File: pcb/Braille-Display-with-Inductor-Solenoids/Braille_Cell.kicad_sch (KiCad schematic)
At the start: 43 parts, among them U10 AD116, U11 AD116, U12 AD116, U13 AD116, U8 AD116, U9 AD116

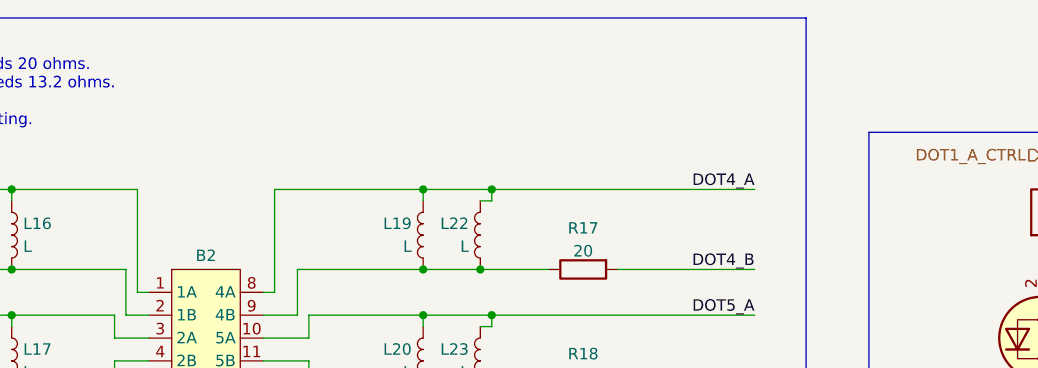
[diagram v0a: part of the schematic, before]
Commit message: Add Rev 2 FIXMEs
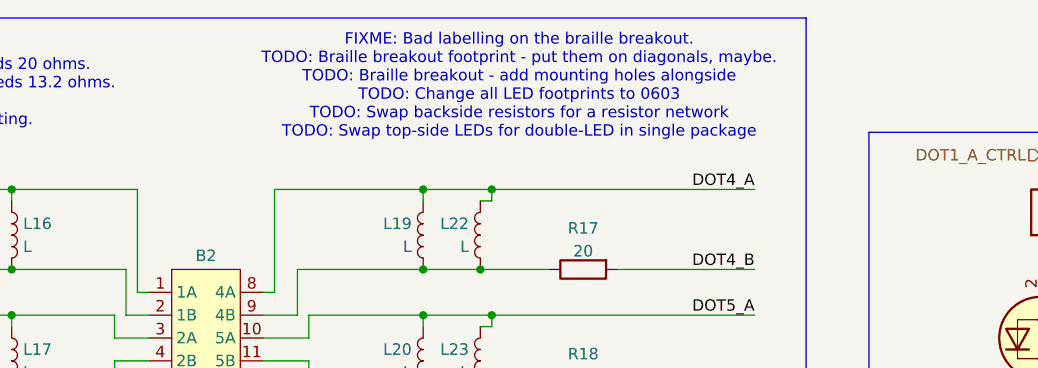
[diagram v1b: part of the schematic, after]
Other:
- note added: "FIXME: Bad labelling on the braille breakout. TODO: Braille breakout footprint - put them on diagonals, maybe. TODO: Braille breakout - add mounting holes alongside TODO: Change all LED footprints to 0603 TODO: Swap backside resistors for a resistor network TODO: Swap top-side LEDs for double-LED in single package"
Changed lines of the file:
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@@
+		)
+	)
+	(text "FIXME: Bad labelling on the braille breakout.\nTODO: Braille breakout footprint - put them on diagonals, maybe.\nTODO: Braille breakout - add mounting holes alongside\nTODO: Change all LED footprints to 0603\nTODO: Swap backside resistors for a resistor network\nTODO: Swap top-side LEDs for double-LED in single package"
+		(exclude_from_sim no)
+		(at 157.988 21.59 0)
+		(effects
+			(font
+				(size 1.27 1.27)
+			)
 		)
 	)

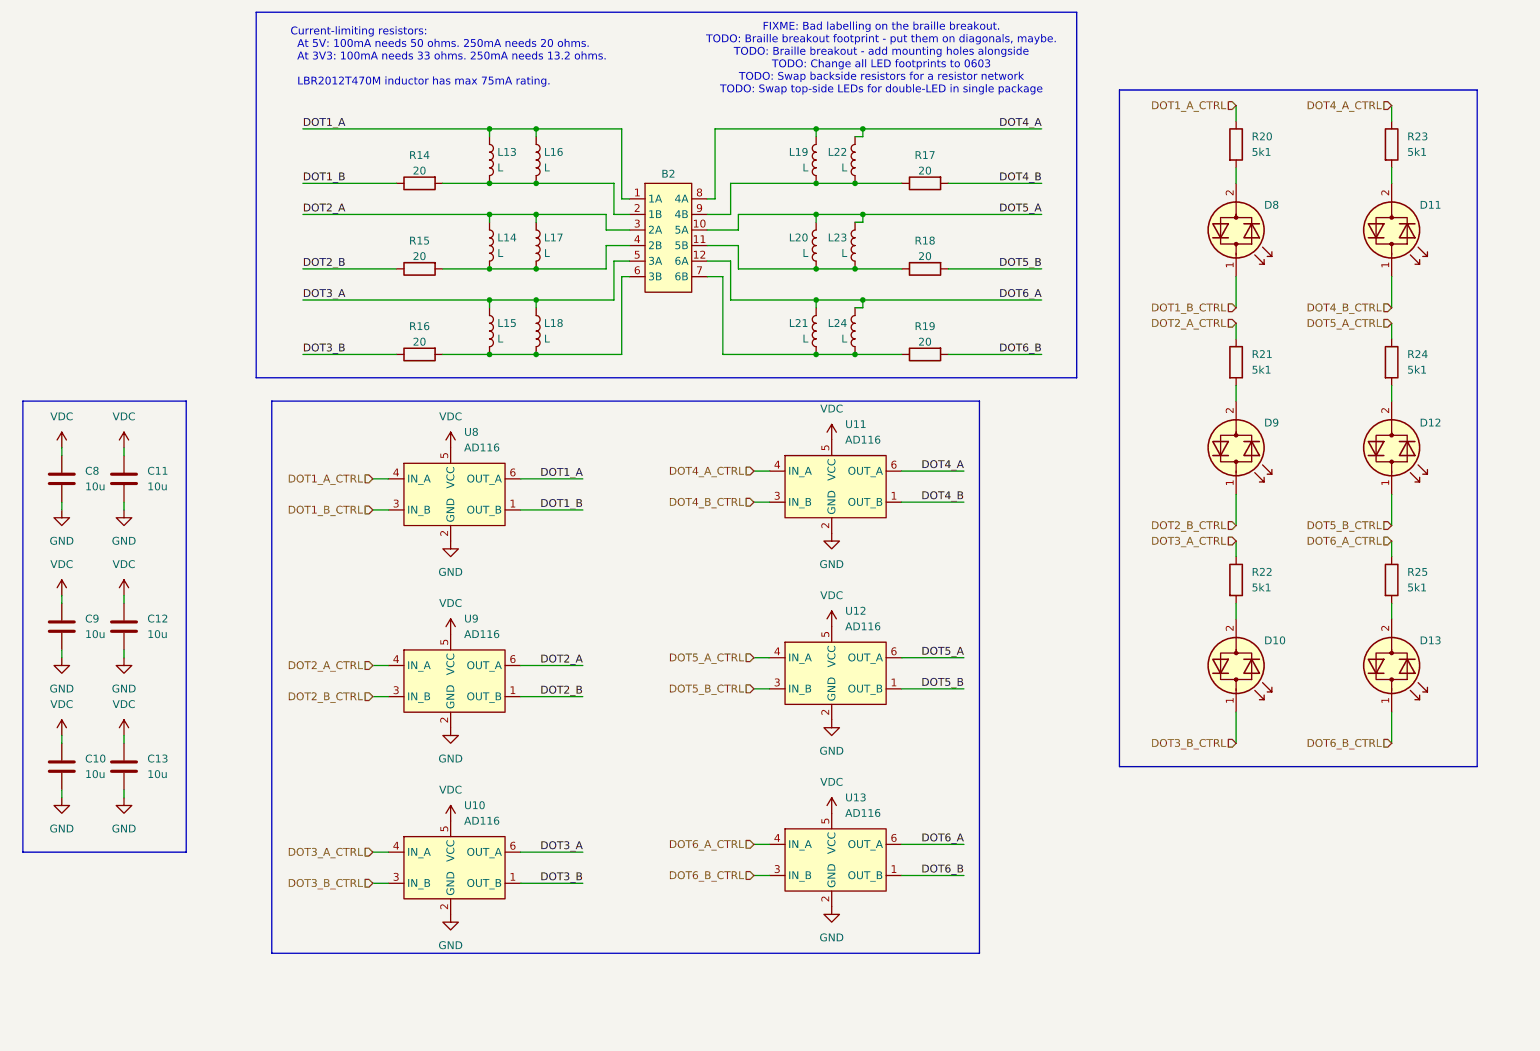
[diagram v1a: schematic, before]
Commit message: WIP (Rev3): Switch to 2 inductors per cell
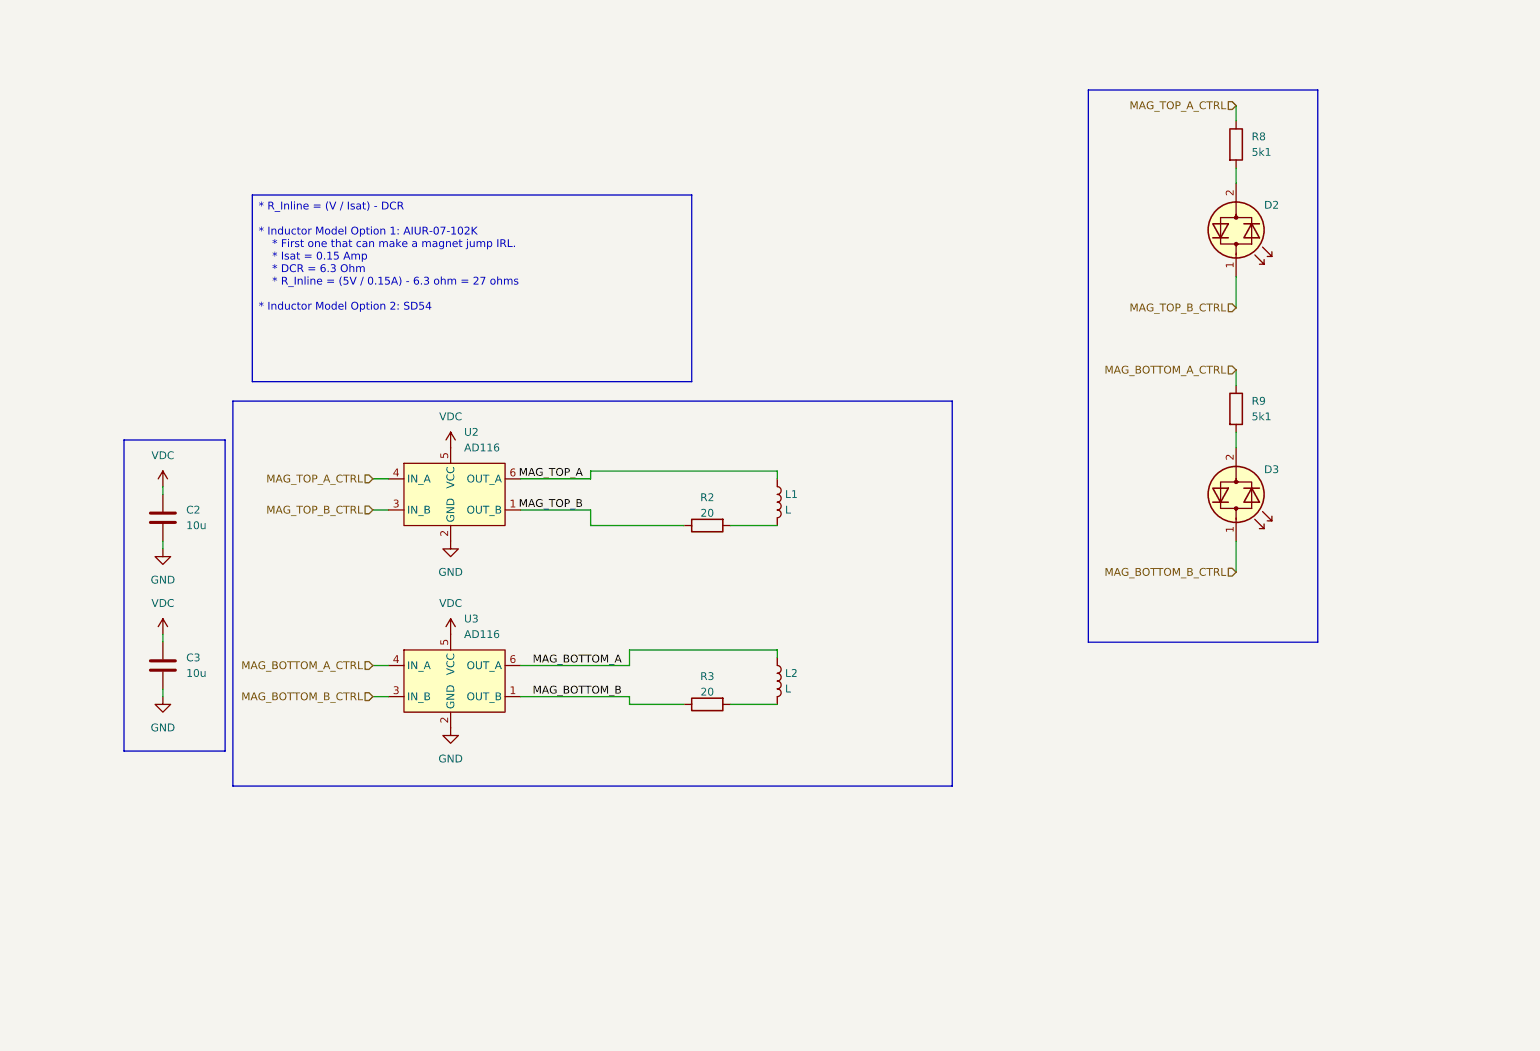
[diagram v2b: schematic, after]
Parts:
- removed B2: ~, 00-project-footprints:Braille_Cell_Breakout, symbol 00-project-symbols:Braille_Cell_Breakout
- removed C10, C11, C12, C13: 10u, Capacitor_SMD:C_1206_3216Metric_Pad1.33x1.80mm_HandSolder, symbol Device:C
- removed D10, D11, D12, D13: LED_Dual_Bidirectional, 00-project-footprints:LED_0603_1608Metric_HandSolder_2x_Reverse, symbol Device:LED_Dual_Bidirectional
- removed L15, L22, L23, L24: L, 00-project-footprints:Inductor_0805_2012Metric_SMD_Vertical_Square_Rev2_1.3mm, symbol Device:L
- removed L16, L17, L18, L19, L20, L21: L, 00-project-footprints:Inductor_VLS201612CX, symbol Device:L
- removed R16, R17, R18, R19: 20, Resistor_SMD:R_0603_1608Metric_Pad0.98x0.95mm_HandSolder, symbol Device:R
- removed R22, R23, R24, R25: 5k1, Resistor_SMD:R_0603_1608Metric_Pad0.98x0.95mm_HandSolder, symbol Device:R
- removed U10, U11, U12, U13: AD116, Package_TO_SOT_SMD:SOT-23-6, symbol 00-project-symbols:AD116_H_Bridge
- L1: renamed from L13; footprint 00-project-footprints:Inductor_0805_2012Metric_SMD_Vertical_Square_Rev2_1.3mm -> 00-project-footprints:Inductor_6mm_AIUR-07-102K_THT_SD54_SMD
- L2: renamed from L14; footprint 00-project-footprints:Inductor_0805_2012Metric_SMD_Vertical_Square_Rev2_1.3mm -> 00-project-footprints:Inductor_6mm_AIUR-07-102K_THT_SD54_SMD
- R2: renamed from R14; footprint Resistor_SMD:R_0603_1608Metric_Pad0.98x0.95mm_HandSolder -> Resistor_SMD:R_2512_6332Metric_Pad1.40x3.35mm_HandSolder
- R3: renamed from R15; footprint Resistor_SMD:R_0603_1608Metric_Pad0.98x0.95mm_HandSolder -> Resistor_SMD:R_2512_6332Metric_Pad1.40x3.35mm_HandSolder
- renumbered C8 to C2, C9 to C3, D8 to D2, D9 to D3, R20 to R8, R21 to R9, U8 to U2, U9 to U3
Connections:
- net DOT1_A renamed MAG_TOP_A
- net DOT1_A_CTRL renamed MAG_TOP_A_CTRL
- net DOT1_B renamed MAG_TOP_B
- net DOT1_B_CTRL renamed MAG_TOP_B_CTRL
- net DOT2_A renamed MAG_BOTTOM_A
- net DOT2_A_CTRL renamed MAG_BOTTOM_A_CTRL
- net DOT2_B renamed MAG_BOTTOM_B
- net DOT2_B_CTRL renamed MAG_BOTTOM_B_CTRL
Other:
- note removed: "Current-limiting resistors: At 5V: 100mA needs 50 ohms. 250mA needs 20 ohms. At 3V3: 100mA needs 33 ohms. 250mA needs 13.2 ohms. LBR2012T470M inductor has max 75mA rating."
- note removed: "FIXME: Bad labelling on the braille breakout. TODO: Braille breakout footprint - put them on diagonals, maybe. TODO: Braille breakout - add mounting holes alongside TODO: Change all LED footprints to 0603 TODO: Swap backside resistors for a resistor network TODO: Swap top-side LEDs for double-LED in single package"
- moved on the sheet: C2, C3, D3, L1, L2, R2, R3, R9

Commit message: WIP: Route one cell
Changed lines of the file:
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@@
+	(wire
+		(pts
+			(xy 87.63 83.82) (xy 87.63 85.09)
+		)
+		(stroke
+			(width 0)
+			(type default)
+		)
+	)
 	(wire
 		(pts
@@
 	(wire
 		(pts
+			(xy 87.63 101.6) (xy 87.63 100.33)
+		)
+		(stroke
+			(width 0)
+			(type default)
+		)
+	)
+	(wire
+		(pts
 			(xy 40.64 100.33) (xy 40.64 101.6)
 		)
@@
 	(wire
 		(pts
+			(xy 87.63 132.08) (xy 87.63 130.81)
+		)
+		(stroke
+			(width 0)
+			(type default)
+		)
+	)
+	(wire
+		(pts
 			(xy 74.93 90.17) (xy 77.47 90.17)
 		)
@@
 		(pts
 			(xy 133.35 127) (xy 140.97 127)
+		)
+		(stroke
+			(width 0)
+			(type default)
+		)
+	)
+	(wire
+		(pts
+			(xy 87.63 114.3) (xy 87.63 115.57)
 		)
 		(stroke
@@
 		(fill
 			(type none)
+		)
+	)
+	(text_box "Driver Options (same pinout):\n\n* BDR6120S - Best\n	* Has flyback diodes\n	* Has TVS gate diodes\n	* 1A continuous, 2.5A peak\n* AD116 - Low Quality (may not have flyback diodes)\n* HD8024H - Most Expensive\n	* Has flyback diodes\n	* 0.8A continuous, 1A peak\n"
+		(exclude_from_sim no)
+		(at 59.055 142.875 0)
+		(size 78.74 22.225)
+		(stroke
+			(width 0)
+			(type default)
+		)
+		(fill
+			(type none)
+		)
+		(effects
+			(font
+				(size 1.27 1.27)
+			)
+			(justify left top)
 		)
 	)
@@
 		)
 	)
+	(netclass_flag ""
+		(length 2.54)
+		(shape round)
+		(at 119.38 127 180)
+		(fields_autoplaced yes)
+		(effects
+			(font
+				(size 1.27 1.27)
+			)
+			(justify right bottom)
+		)
+		(property "Netclass" "Switched_Power"
+			(at 120.0785 129.54 0)
+			(effects
+				(font
+					(size 1.27 1.27)
+					(italic yes)
+				)
+				(justify left)
+			)
+		)
+	)
+	(netclass_flag ""
+		(length 2.54)
+		(shape round)
+		(at 134.62 97.79 180)
+		(fields_autoplaced yes)
+		(effects
+			(font
+				(size 1.27 1.27)
+			)
+			(justify right bottom)
+		)
+		(property "Netclass" "Switched_Power"
+			(at 135.3185 100.33 0)
+			(effects
+				(font
+					(size 1.27 1.27)
+					(italic yes)
+				)
+				(justify left)
+			)
+		)
+	)
+	(netclass_flag ""
+		(length 2.54)
+		(shape round)
+		(at 138.43 127 180)
+		(fields_autoplaced yes)
+		(effects
+			(font
+				(size 1.27 1.27)
+			)
+			(justify right bottom)
+		)
+		(property "Netclass" "Switched_Power"
+			(at 139.1285 129.54 0)
+			(effects
+				(font
+					(size 1.27 1.27)
+					(italic yes)
+				)
+				(justify left)
+			)
+		)
+	)
+	(netclass_flag ""
+		(length 2.54)
+		(shape round)
+		(at 115.57 88.9 0)
+		(fields_autoplaced yes)
+		(effects
+			(font
+				(size 1.27 1.27)
+			)
+			(justify left bottom)
+		)
+		(property "Netclass" "Switched_Power"
+			(at 116.2685 86.36 0)
+			(effects
+				(font
+					(size 1.27 1.27)
+					(italic yes)
+				)
+				(justify left)
+			)
+		)
+	)
+	(netclass_flag ""
+		(length 2.54)
+		(shape round)
+		(at 114.3 97.79 180)
+		(fields_autoplaced yes)
+		(effects
+			(font
+				(size 1.27 1.27)
+			)
+			(justify right bottom)
+		)
+		(property "Netclass" "Switched_Power"
+			(at 114.9985 100.33 0)
+			(effects
+				(font
+					(size 1.27 1.27)
+					(italic yes)
+				)
+				(justify left)
+			)
+		)
+	)
+	(netclass_flag ""
+		(length 2.54)
+		(shape round)
+		(at 120.65 118.11 0)
+		(fields_autoplaced yes)
+		(effects
+			(font
+				(size 1.27 1.27)
+			)
+			(justify left bottom)
+		)
+		(property "Netclass" "Switched_Power"
+			(at 121.3485 115.57 0)
+			(effects
+				(font
+					(size 1.27 1.27)
+					(italic yes)
+				)
+				(justify left)
+			)
+		)
+	)
 	(symbol
 		(lib_id "power:VDC")
-		(at 87.63 115.57 0)
+		(at 87.63 114.3 0)
 		(unit 1)
 		(exclude_from_sim no)
@@
 		(fields_autoplaced yes)
 		(property "Reference" "#PWR031"
-			(at 87.63 119.38 0)
+			(at 87.63 118.11 0)
 			(effects
 				(font
@@
 		)
 		(property "Value" "VDC"
-			(at 87.63 110.49 0)
+			(at 87.63 109.22 0)
 			(effects
 				(font
@@
 		)
 		(property "Footprint" ""
-			(at 87.63 115.57 0)
+			(at 87.63 114.3 0)
 			(effects
 				(font
@@
 		)
 		(property "Datasheet" ""
-			(at 87.63 115.57 0)
+			(at 87.63 114.3 0)
 			(effects
 				(font
@@
 		)
 		(property "Description" "Power symbol creates a global label with name \"VDC\""
-			(at 87.63 115.57 0)
+			(at 87.63 114.3 0)
 			(effects
 				(font
@@
 	(symbol
 		(lib_id "power:VDC")
-		(at 87.63 85.09 0)
+		(at 87.63 83.82 0)
 		(unit 1)
 		(exclude_from_sim no)
@@
 		(fields_autoplaced yes)
 		(property "Reference" "#PWR029"
-			(at 87.63 88.9 0)
+			(at 87.63 87.63 0)
 			(effects
 				(font
@@
 		)
 		(property "Value" "VDC"
-			(at 87.63 80.01 0)
+			(at 87.63 78.74 0)
 			(effects
 				(font
@@
 		)
 		(property "Footprint" ""
-			(at 87.63 85.09 0)
+			(at 87.63 83.82 0)
 			(effects
 				(font
@@
 		)
 		(property "Datasheet" ""
-			(at 87.63 85.09 0)
+			(at 87.63 83.82 0)
 			(effects
 				(font
@@
 		)
 		(property "Description" "Power symbol creates a global label with name \"VDC\""
-			(at 87.63 85.09 0)
+			(at 87.63 83.82 0)
 			(effects
 				(font
@@
 	(symbol
 		(lib_id "power:GND")
-		(at 87.63 130.81 0)
+		(at 87.63 132.08 0)
 		(unit 1)
 		(exclude_from_sim no)
@@
 		(fields_autoplaced yes)
 		(property "Reference" "#PWR032"
+			(at 87.63 138.43 0)
+			(effects
+				(font
+					(size 1.27 1.27)
+				)
+				(hide yes)
+			)
+		)
+		(property "Value" "GND"
 			(at 87.63 137.16 0)
 			(effects
@@
 					(size 1.27 1.27)
 				)
-				(hide yes)
-			)
-		)
-		(property "Value" "GND"
-			(at 87.63 135.89 0)
-			(effects
-				(font
-					(size 1.27 1.27)
-				)
 			)
 		)
 		(property "Footprint" ""
-			(at 87.63 130.81 0)
+			(at 87.63 132.08 0)
 			(effects
 				(font
@@
 		)
 		(property "Datasheet" ""
-			(at 87.63 130.81 0)
+			(at 87.63 132.08 0)
 			(effects
 				(font
@@
 		)
 		(property "Description" "Power symbol creates a global label with name \"GND\" , ground"
-			(at 87.63 130.81 0)
+			(at 87.63 132.08 0)
 			(effects
 				(font
@@
 	(symbol
 		(lib_id "power:GND")
-		(at 87.63 100.33 0)
+		(at 87.63 101.6 0)
 		(unit 1)
 		(exclude_from_sim no)
@@
 		(fields_autoplaced yes)
 		(property "Reference" "#PWR030"
+			(at 87.63 107.95 0)
+			(effects
+				(font
+					(size 1.27 1.27)
+				)
+				(hide yes)
+			)
+		)
+		(property "Value" "GND"
 			(at 87.63 106.68 0)
 			(effects
@@
 					(size 1.27 1.27)
 				)
-				(hide yes)
-			)
-		)
-		(property "Value" "GND"
-			(at 87.63 105.41 0)
-			(effects
-				(font
-					(size 1.27 1.27)
-				)
 			)
 		)
 		(property "Footprint" ""
-			(at 87.63 100.33 0)
+			(at 87.63 101.6 0)
 			(effects
 				(font
@@
 		)
 		(property "Datasheet" ""
-			(at 87.63 100.33 0)
+			(at 87.63 101.6 0)
 			(effects
 				(font
@@
 		)
 		(property "Description" "Power symbol creates a global label with name \"GND\" , ground"
-			(at 87.63 100.33 0)
-			(effects
-				(font
+			(at 87.63 101.6 0)
+			(effects
+				(font
